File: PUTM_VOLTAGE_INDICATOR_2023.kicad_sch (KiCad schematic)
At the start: 29 parts

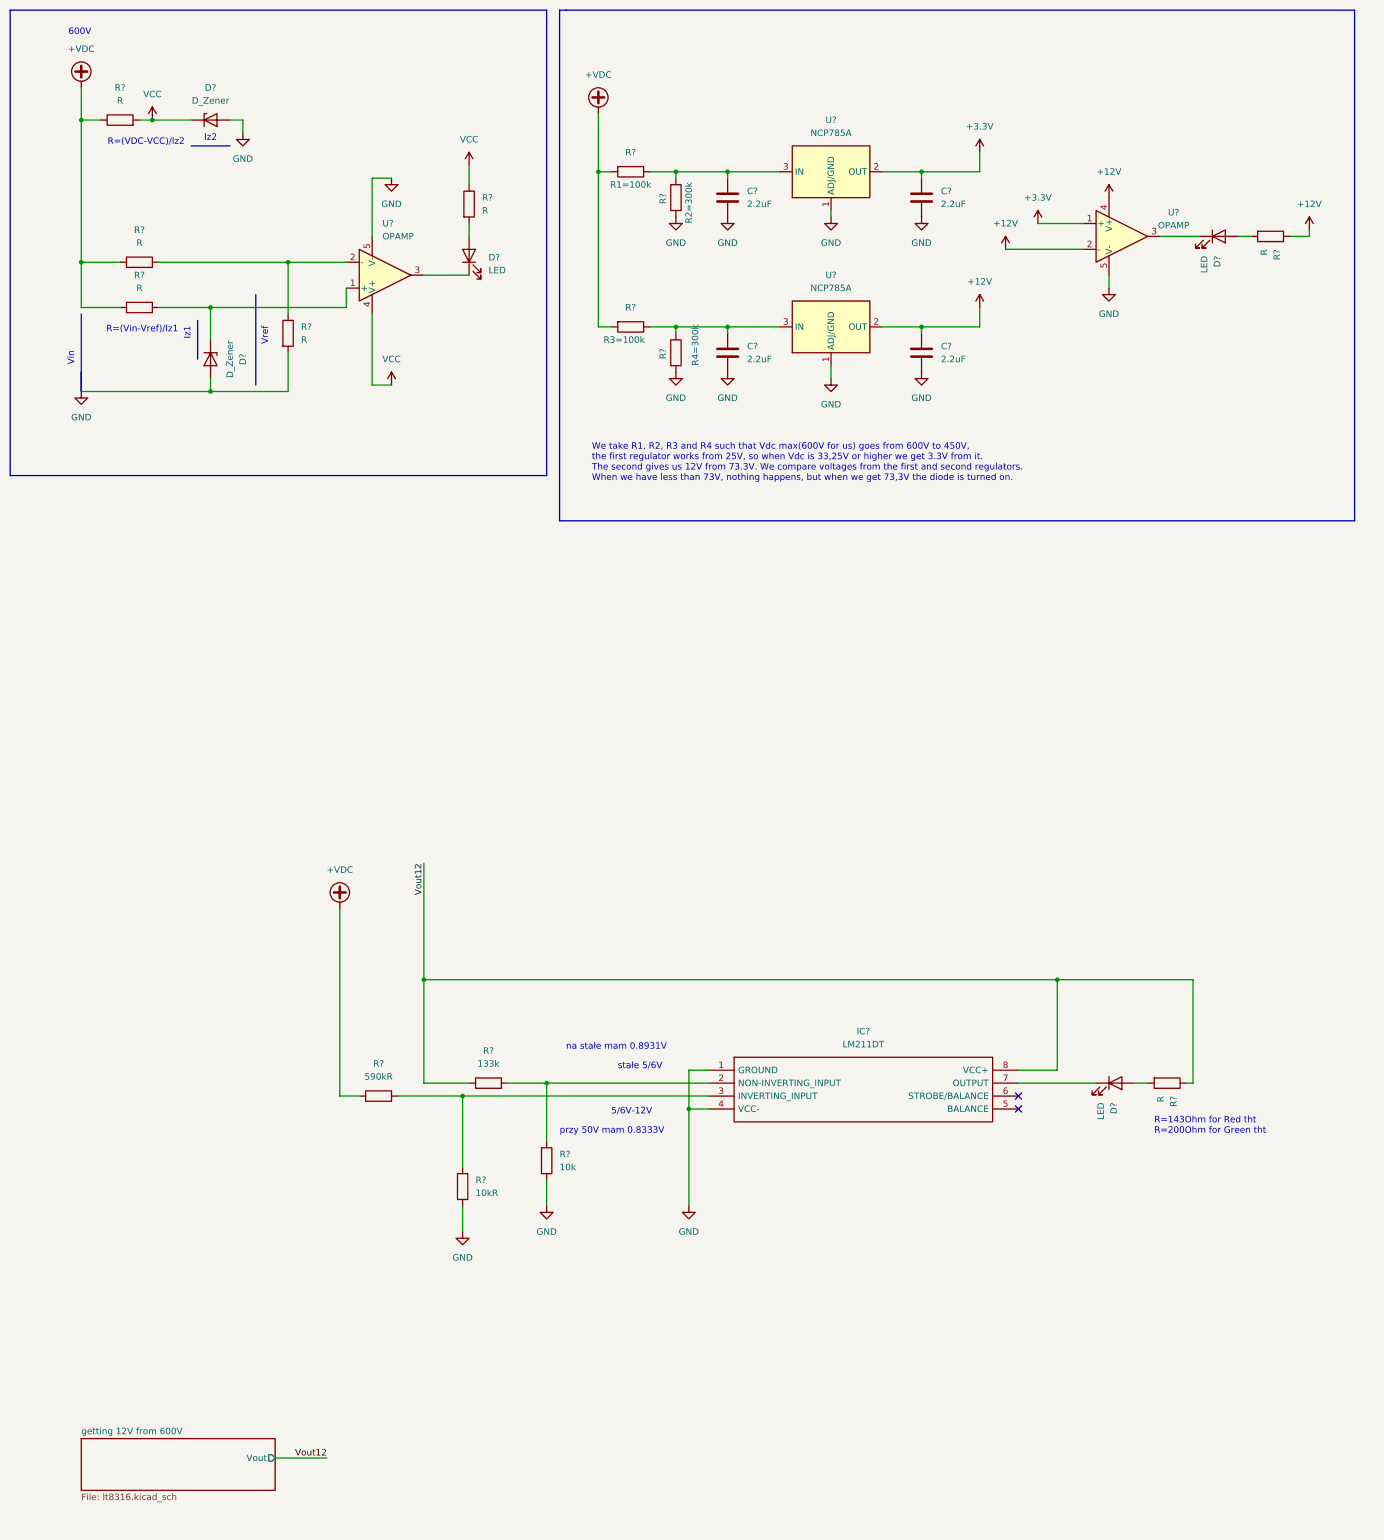
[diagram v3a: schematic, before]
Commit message: dodaję fus, wybieram led, zmieniam komparator, dodaję datasheety
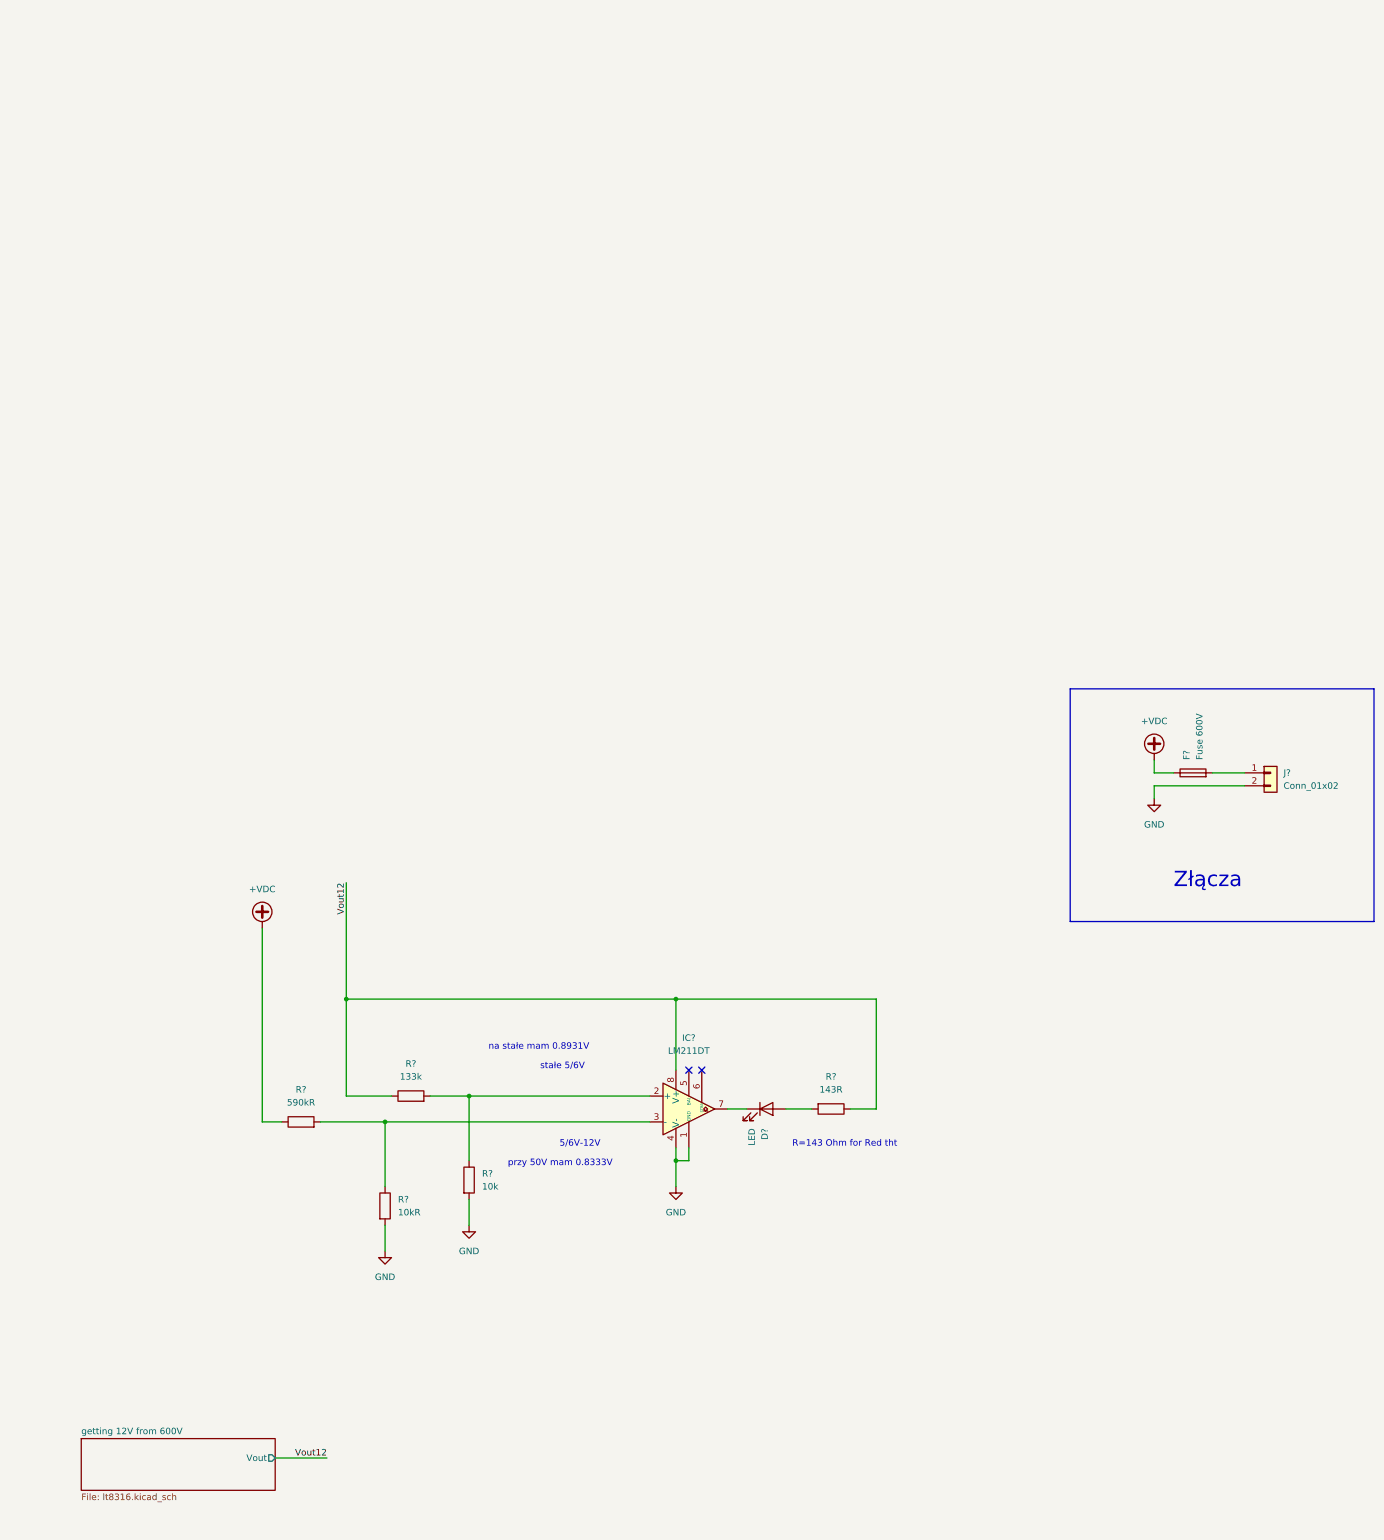
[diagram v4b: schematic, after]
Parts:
- removed C? (x4): 2.2uF, symbol Device:C
- removed D? (x2): LED, symbol Device:LED
- removed D? (x2): D_Zener, symbol Device:D_Zener
- removed R?: R4=300k, symbol Device:R
- removed R? (x6): R, symbol Device:R
- removed R?: R2=300k, symbol Device:R
- removed R?: R3=100k, symbol Device:R
- removed R?: R1=100k, symbol Device:R
- removed U? (x2): NCP785A, Package_TO_SOT_SMD:SOT-89-3, symbol Regulator_Linear:LD1086DT25TR
- removed U? (x2): OPAMP, symbol pspice:OPAMP
- added F?: Fuse 600V, symbol Device:Fuse
- added J?: Conn_01x02, symbol Connector_Generic:Conn_01x02
- D?: footprint (none) -> LED_THT:LED_D2.0mm_W4.8mm_H2.5mm_FlatTop
- IC?: symbol Voltage_indicator:LM211DT -> Comparator:LM311
- R?: value R -> 143R
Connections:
- net +VDC: now also F?.1
- net GND: now also J?.2 (Pin_2)
- new net: F?.2, J?.1 (Pin_1)
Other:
- note added: "R=143 Ohm for Red tht"
- note added: "Złącza"
- note removed: "600V"
- note removed: "Iz1"
- note removed: "Iz2"
- note removed: "R=(VDC-VCC)/Iz2"
- note removed: "R=(Vin-Vref)/Iz1"
- note removed: "R=143Ohm for Red tht R=200Ohm for Green tht"
- note removed: "Vin"
- note removed: "Vref"
- note removed: "We take R1, R2, R3 and R4 such that Vdc max(600V for us) goes from 600V to 450V, the first regulator works from 25V, so when Vdc is 33,25V or higher we get 3.3V from it. The second gives us 12V from 73.3V. We compare voltages from the first and second regulators. When we have less than 73V, nothing happens, but when we get 73,3V the diode is turned on."
- moved on the sheet: D?, R?

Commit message: add resistors / add footprints and datasheets/ change symbols
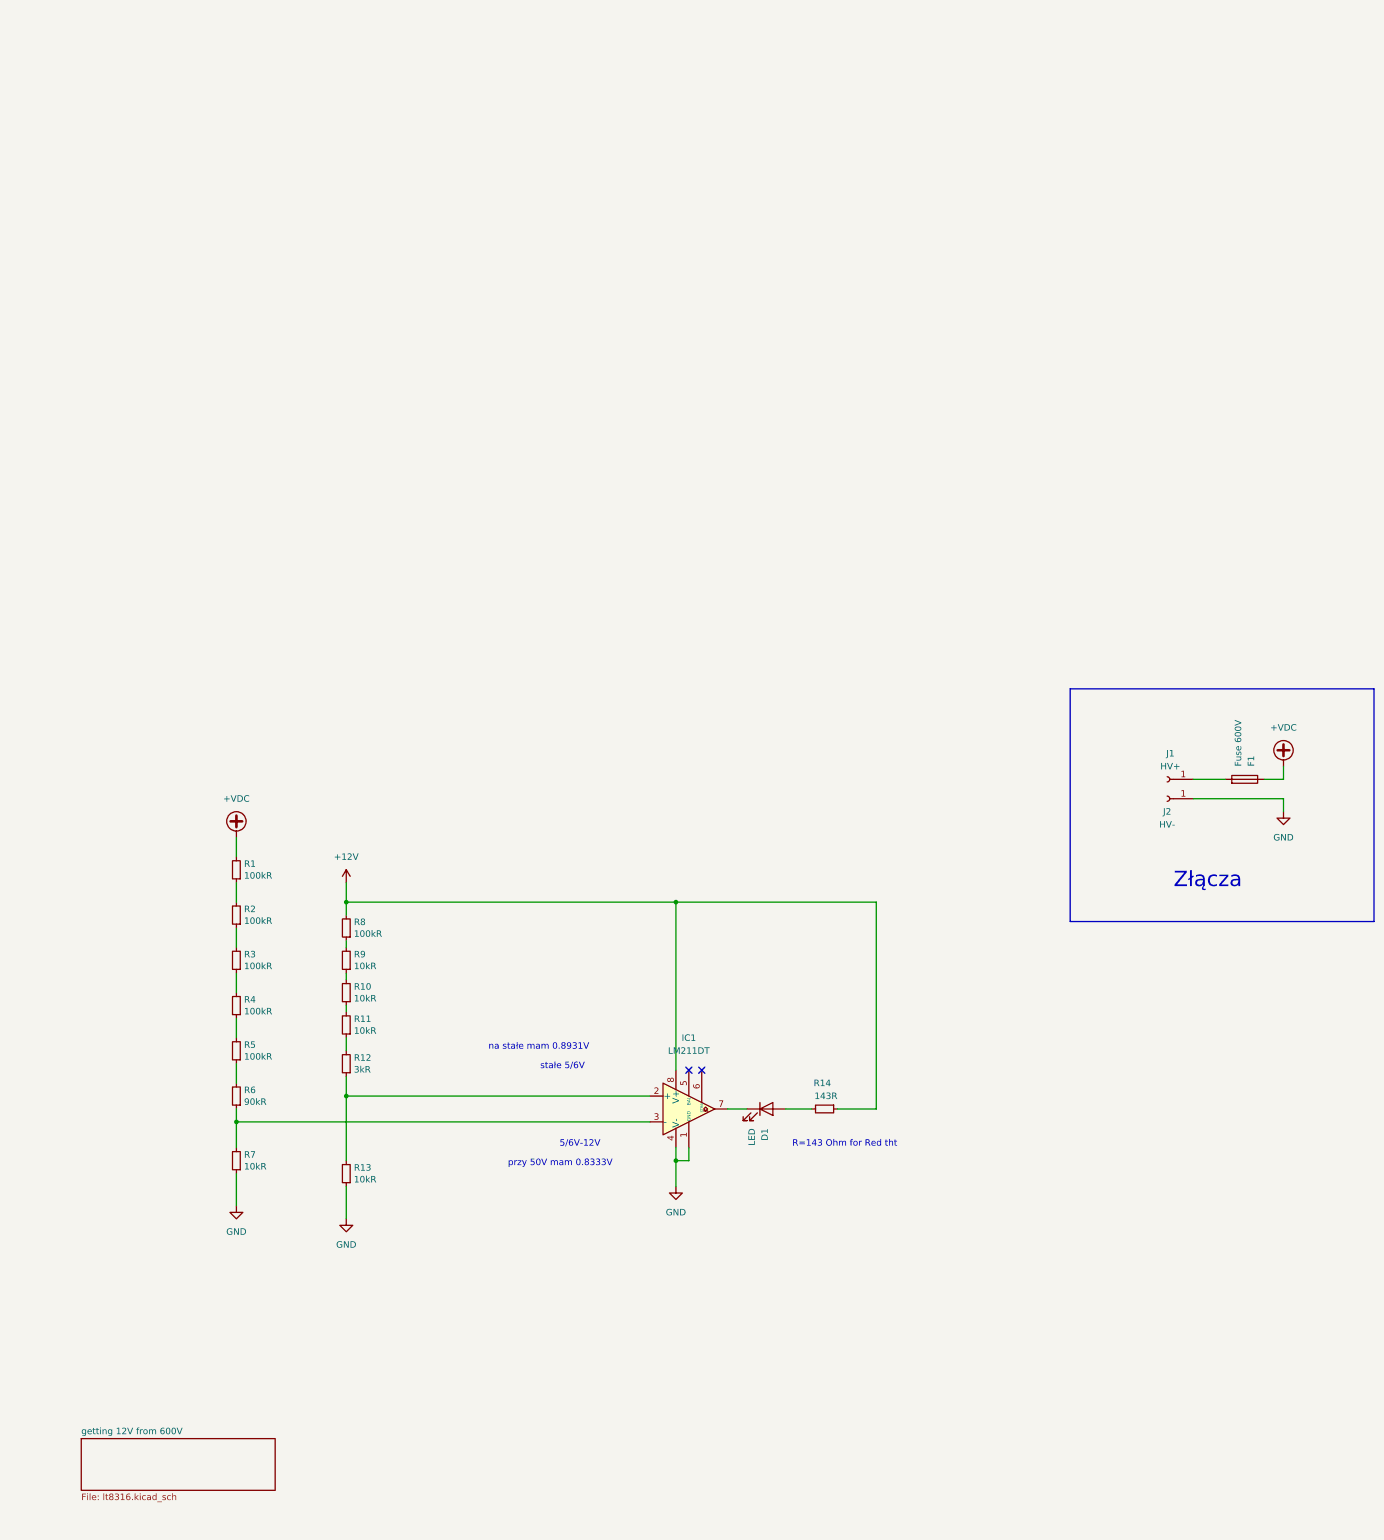
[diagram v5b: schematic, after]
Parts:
- removed J?: Conn_01x02, symbol Connector_Generic:Conn_01x02
- removed R?: 590kR, symbol Device:R
- removed R?: 133k, symbol Device:R
- removed R?: 10kR, symbol Device:R
- removed R?: 10k, symbol Device:R
- removed R?: 143R, symbol Device:R
- added J1: HV+, Connector_Wire:SolderWire-0.5sqmm_1x01_D0.9mm_OD2.1mm_Relief, symbol Connector:Conn_01x01_Female
- added J2: HV-, Connector_Wire:SolderWire-0.5sqmm_1x01_D0.9mm_OD2.1mm_Relief, symbol Connector:Conn_01x01_Female
- added R1, R2, R3, R4, R5, R8: 100kR, Resistor_SMD:R_1206_3216Metric, symbol Device:R_Small
- added R10, R11, R13, R7, R9: 10kR, Resistor_SMD:R_1206_3216Metric, symbol Device:R_Small
- added R12: 3kR, Resistor_SMD:R_1206_3216Metric, symbol Device:R_Small
- added R14: 143R, Resistor_SMD:R_1206_3216Metric, symbol Device:R_Small
- added R6: 90kR, Resistor_SMD:R_1206_3216Metric, symbol Device:R_Small
- F1: renamed from F?; footprint (none) -> Fuse:Fuseholder_Cylinder-6.3x32mm_Schurter_0031-8002_Horizontal_Open
- IC1: renamed from IC?; footprint SOIC127P600X175-8N -> Package_SO:SO-8_3.9x4.9mm_P1.27mm
- gave numbers to parts that had none: 1
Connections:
- net +VDC: now also R1.2
- net GND: now also J2.1 (Pin_1), R13.1, R7.1
- net at IC1.3 (-): now also R6.1, R7.2
- net at F1.2: now also J1.1 (Pin_1)
- net at IC1.2 (+): now also R12.1, R13.2
- net at D1.2 (A): now also R14.2
- net Vout12 renamed +12V
- net +12V: now also R14.1, R8.2
- new net: R3.1, R4.2
- new net: R2.1, R3.2
- new net: R10.2, R9.1
- new net: R8.1, R9.2
- new net: R11.1, R12.2
- new net: R1.1, R2.2
- new net: R10.1, R11.2
- new net: R4.1, R5.2
- new net: R5.1, R6.2
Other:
- sheet getting 12V from 600V ports: added none; removed Vout
- moved on the sheet: F1

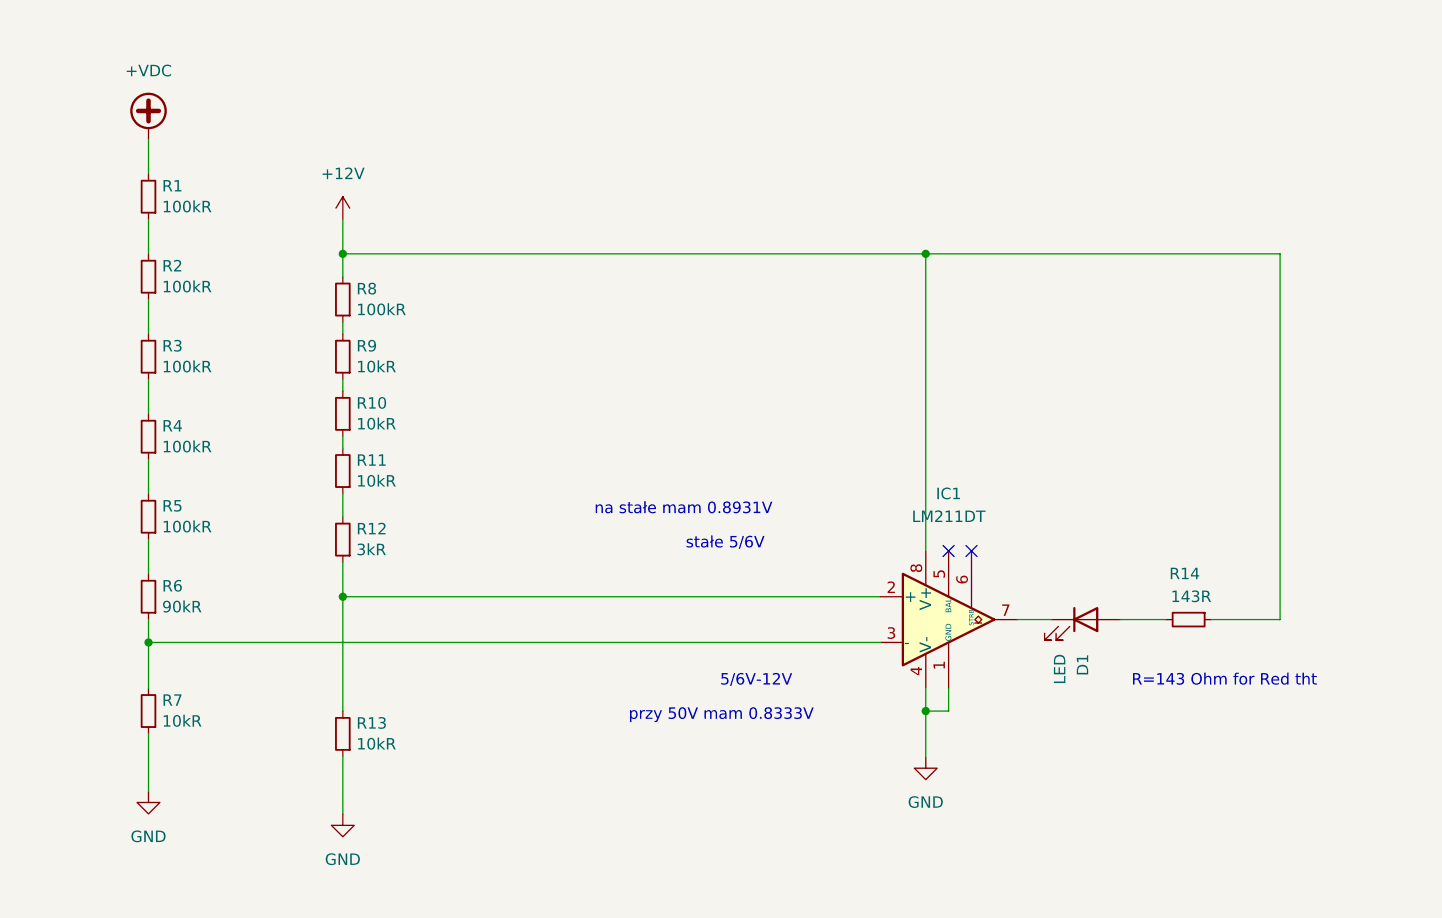
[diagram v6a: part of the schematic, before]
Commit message: resistors change; elements placed; new footprints
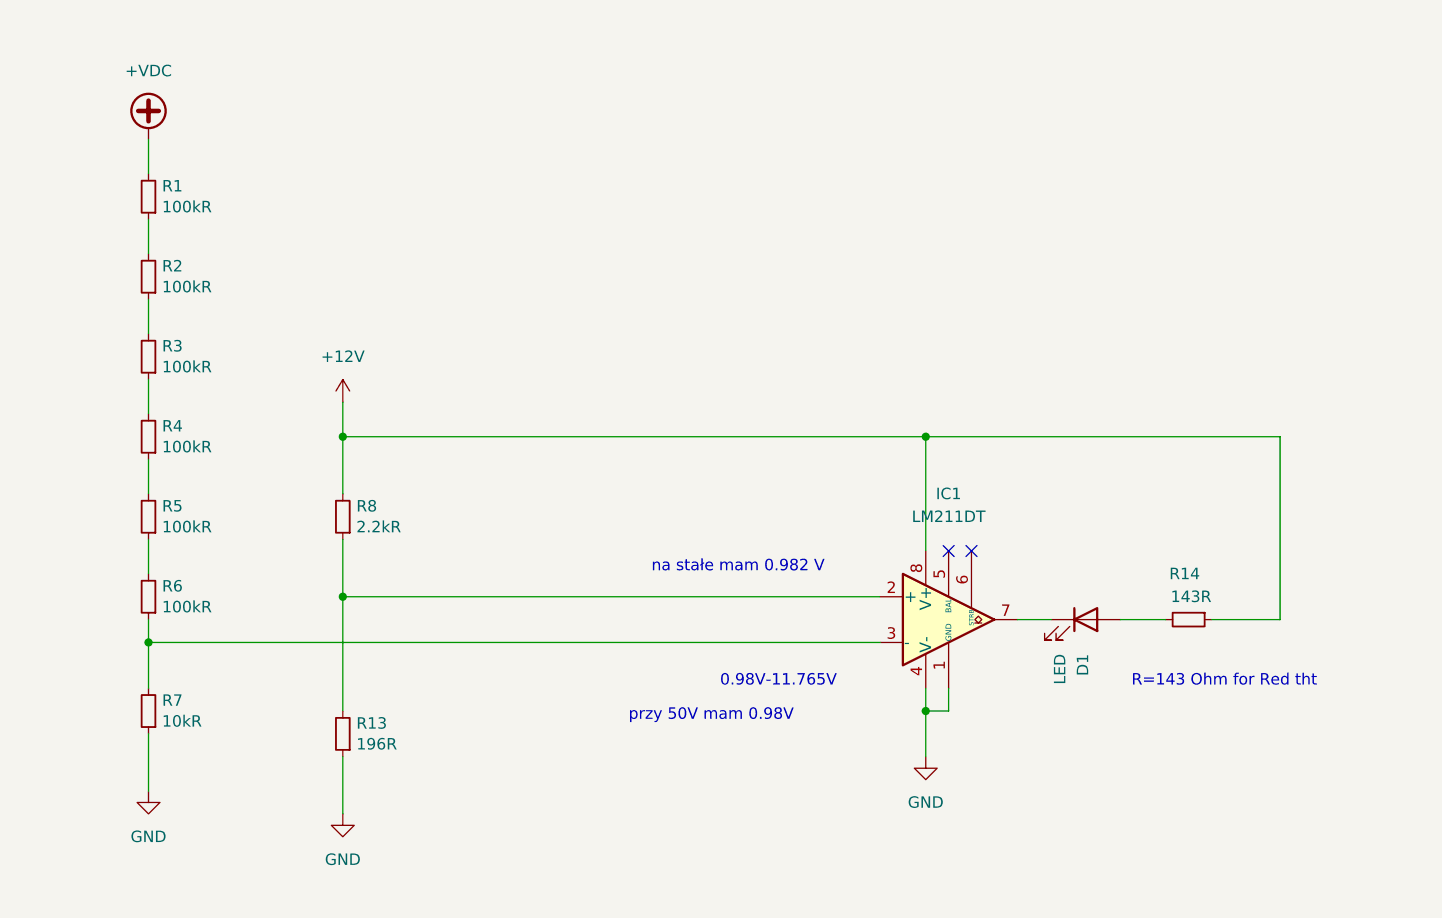
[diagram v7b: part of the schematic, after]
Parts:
- removed R10, R11, R9: 10kR, Resistor_SMD:R_1206_3216Metric, symbol Device:R_Small
- removed R12: 3kR, Resistor_SMD:R_1206_3216Metric, symbol Device:R_Small
- F1: footprint Fuse:Fuseholder_Cylinder-6.3x32mm_Schurter_0031-8002_Horizontal_Open -> vindicator:01020071Z-FUSE-CLIP
- R13: value 10kR -> 196R; footprint Resistor_SMD:R_1206_3216Metric -> Resistor_SMD:R_0603_1608Metric
- R14: footprint Resistor_SMD:R_1206_3216Metric -> Resistor_SMD:R_0603_1608Metric
- R6: value 90kR -> 100kR
- R8: value 100kR -> 2.2kR; footprint Resistor_SMD:R_1206_3216Metric -> Resistor_SMD:R_0603_1608Metric
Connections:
- net at R8.1: now also IC1.2 (+), R13.2
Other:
- note added: "0.98V-11.765V"
- note added: "na stałe mam 0.982 V"
- note added: "przy 50V mam 0.98V"
- note removed: "5/6V-12V"
- note removed: "na stałe mam 0.8931V"
- note removed: "przy 50V mam 0.8333V"
- note removed: "stałe 5/6V"
- moved on the sheet: R8
